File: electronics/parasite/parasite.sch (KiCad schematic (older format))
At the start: 24 parts, among them Q1 MMBT3904, Q2 MMBT3904, Q3 AO3407A, U1 E73-2G4M04S1B

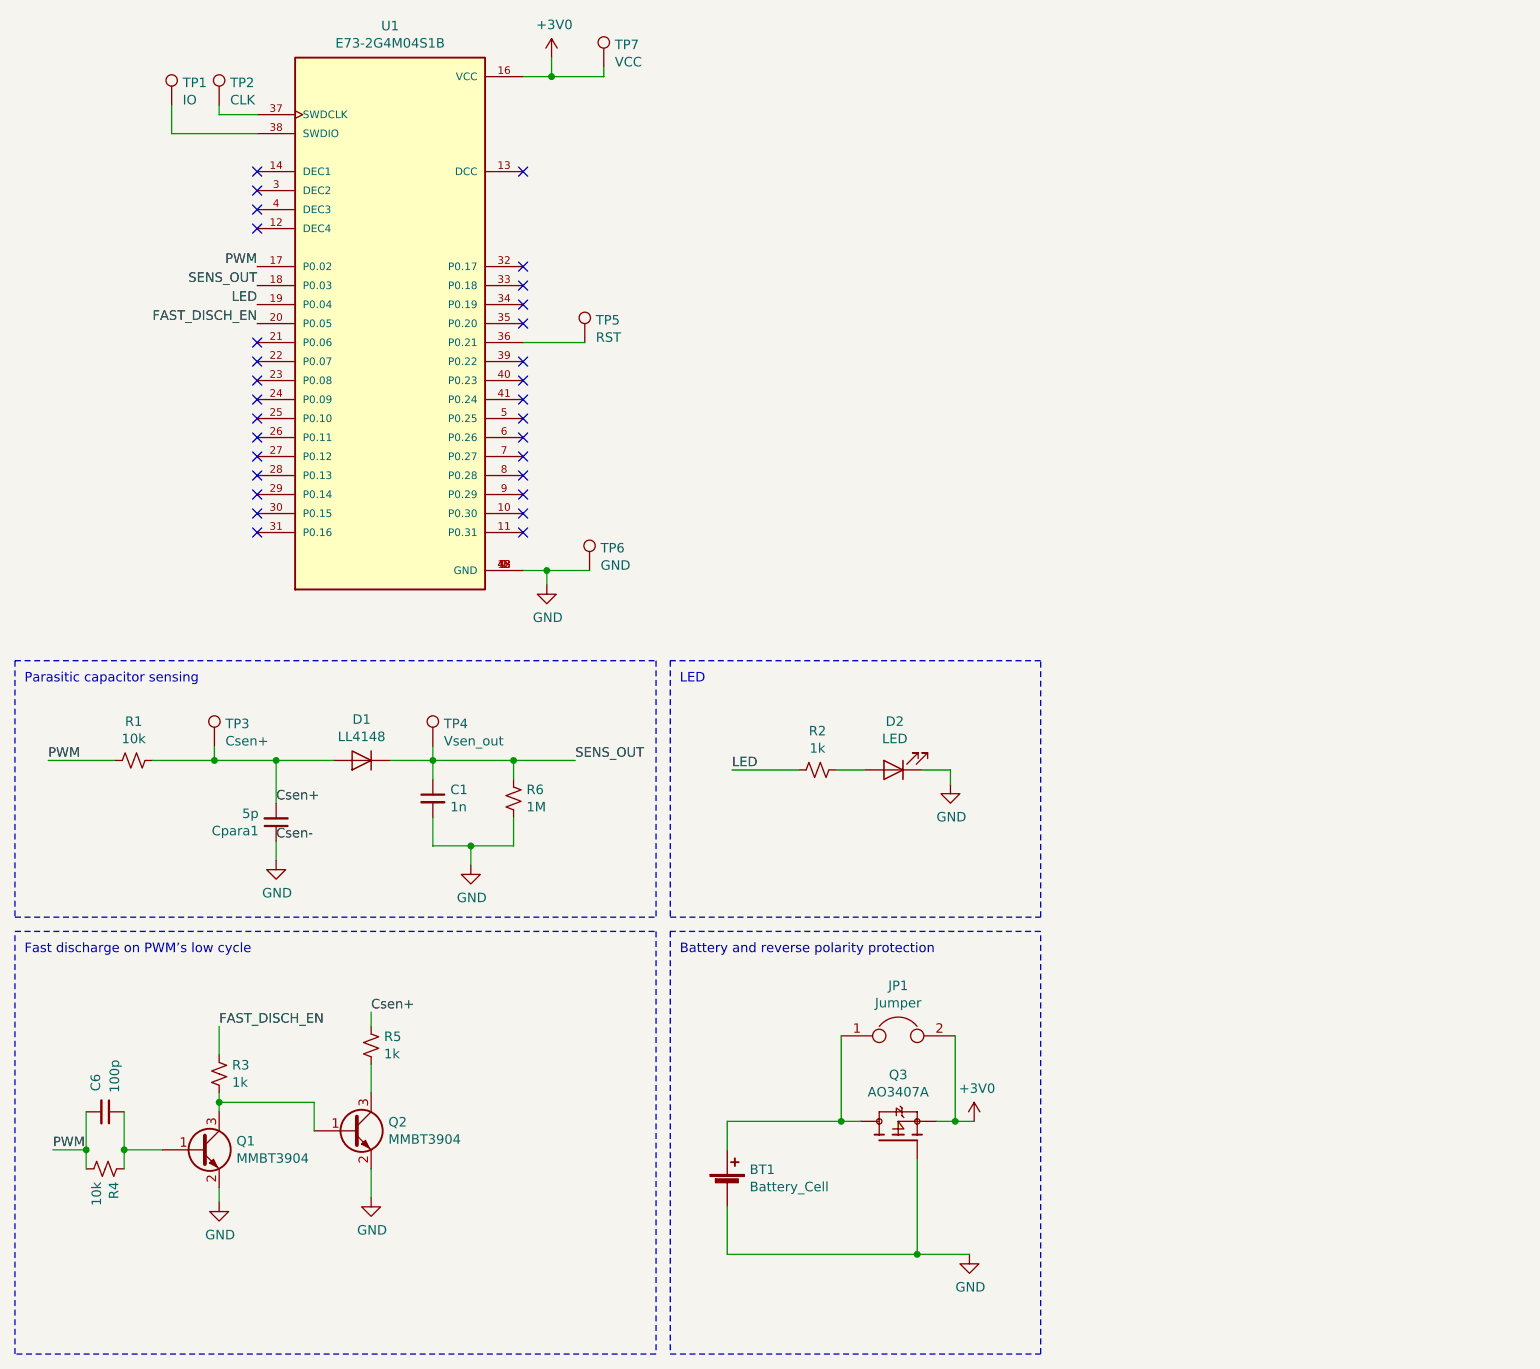
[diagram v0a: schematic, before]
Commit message: Adds sht30 temperature and humidity sensor
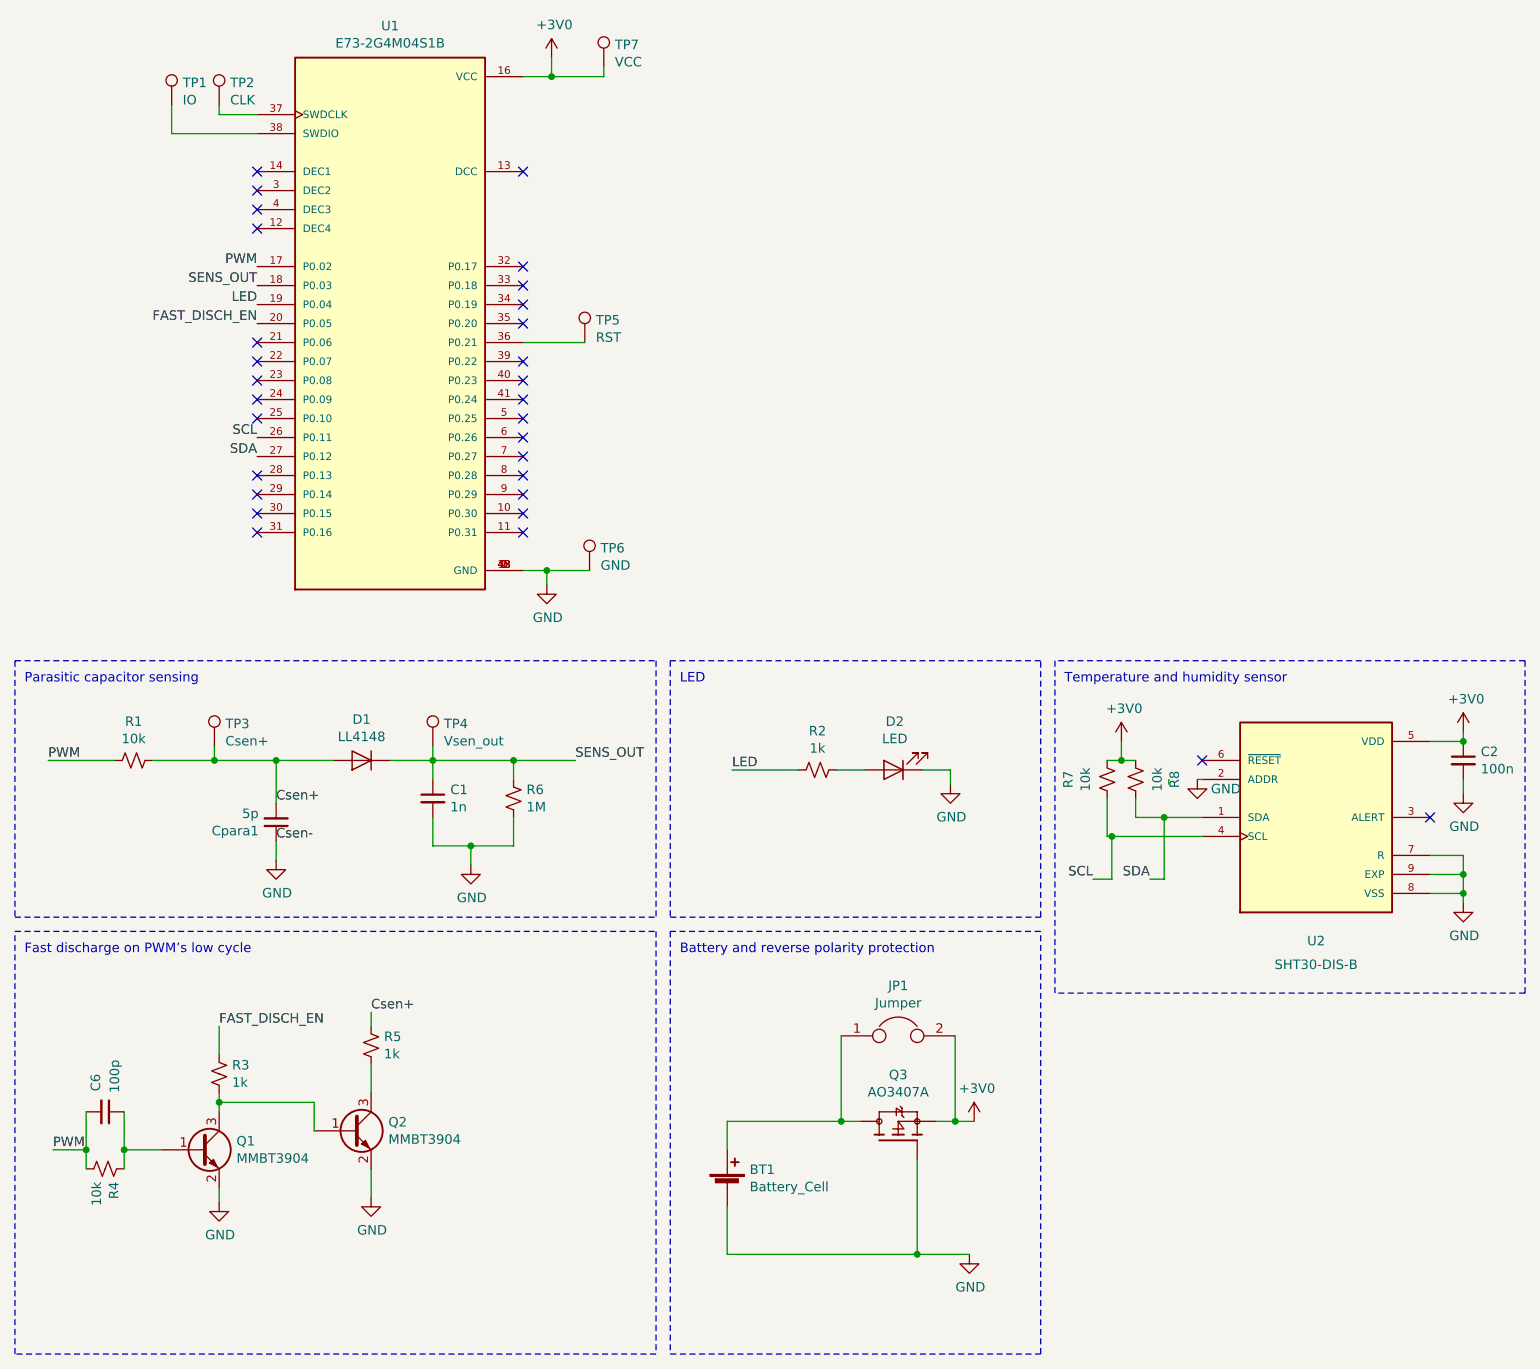
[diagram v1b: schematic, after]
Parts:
- added C2: 100n, Capacitor_SMD:C_0805_2012Metric, symbol Device:C_Small
- added R7, R8: 10k, Resistor_SMD:R_0805_2012Metric, symbol Device:R_Small_US
- added U2: SHT30-DIS-B, DFN250X250X100-9N, symbol SHT30-DIS-B:SHT30-DIS-B
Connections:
- net +3V0: now also C2.1, R7.2, R8.1, U2.5 (VDD)
- net GND: now also C2.2, U2.2 (ADDR), U2.7 (R), U2.8 (VSS), U2.9 (EXP)
- net SCL: now reaches U1.26 (P0.11)
- net SCL: now also R7.1, U2.4 (SCL)
- net SDA: now reaches U1.27 (P0.12)
- net SDA: now also R8.2, U2.1 (SDA)
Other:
- note added: "Temperature and humidity sensor"
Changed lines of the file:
@@
 NoConn ~ 1950 2650
 NoConn ~ 1950 2750
-NoConn ~ 1950 2850
-NoConn ~ 1950 2950
 NoConn ~ 1950 3050
 NoConn ~ 1950 3150
@@
 	1    0    0    -1
 $EndComp
+$Comp
+L SHT30-DIS-B:SHT30-DIS-B U2
+U 1 1 603581DD
+P 7525 4850
+F 0 "U2" H 7525 4200 50  0000 C CNN
+F 1 "SHT30-DIS-B" H 7525 4075 50  0000 C CNN
+F 2 "DFN250X250X100-9N" H 7525 4850 50  0001 L BNN
+F 3 "" H 7525 4850 50  0001 L BNN
+F 4 "Sensirion" H 7525 4850 50  0001 L BNN "MANUFACTURER"
+	1    7525 4850
+	1    0    0    -1
+$EndComp
+$Comp
+L power:+3V0 #PWR0106
+U 1 1 60359DB4
+P 8300 4400
+F 0 "#PWR0106" H 8300 4250 50  0001 C CNN
+F 1 "+3V0" H 8315 4573 50  0000 C CNN
+F 2 "" H 8300 4400 50  0001 C CNN
+F 3 "" H 8300 4400 50  0001 C CNN
+	1    8300 4400
+	1    0    0    -1
+$EndComp
+Wire Wire Line
+	8125 4450 8300 4450
+Wire Wire Line
+	8300 4450 8300 4400
+$Comp
+L power:GND #PWR0107
+U 1 1 6035C6F6
+P 8300 5300
+F 0 "#PWR0107" H 8300 5050 50  0001 C CNN
+F 1 "GND" H 8305 5127 50  0000 C CNN
+F 2 "" H 8300 5300 50  0001 C CNN
+F 3 "" H 8300 5300 50  0001 C CNN
+	1    8300 5300
+	1    0    0    -1
+$EndComp
+Wire Wire Line
+	8125 5250 8300 5250
+Wire Wire Line
+	8300 5250 8300 5300
+Wire Wire Line
+	8125 5050 8300 5050
+Wire Wire Line
+	8300 5050 8300 5150
+Connection ~ 8300 5250
+Wire Wire Line
+	8125 5150 8300 5150
+Connection ~ 8300 5150
+Wire Wire Line
+	8300 5150 8300 5250
+$Comp
+L power:GND #PWR0108
+U 1 1 60360ACA
+P 6900 4650
+F 0 "#PWR0108" H 6900 4400 50  0001 C CNN
+F 1 "GND" H 7050 4600 50  0000 C CNN
+F 2 "" H 6900 4650 50  0001 C CNN
+F 3 "" H 6900 4650 50  0001 C CNN
+	1    6900 4650
+	1    0    0    -1
+$EndComp
+NoConn ~ 6925 4550
+NoConn ~ 8125 4850
+Text Label 1950 2950 2    50   ~ 0
+SDA
+Text Label 1950 2850 2    50   ~ 0
+SCL
+Text Label 6350 5175 2    50   ~ 0
+SCL
+Wire Notes Line
+	8625 4025 6150 4025
+Text Notes 6200 4150 0    50   ~ 0
+Temperature and humidity sensor
+$Comp
+L Device:C_Small C2
+U 1 1 6036F153
+P 8300 4550
+F 0 "C2" H 8392 4596 50  0000 L CNN
+F 1 "100n" H 8392 4505 50  0000 L CNN
+F 2 "Capacitor_SMD:C_0805_2012Metric" H 8300 4550 50  0001 C CNN
+F 3 "~" H 8300 4550 50  0001 C CNN
+	1    8300 4550
+	1    0    0    -1
+$EndComp
+Connection ~ 8300 4450
+$Comp
+L power:GND #PWR0109
+U 1 1 6036FCD2
+P 8300 4725
+F 0 "#PWR0109" H 8300 4475 50  0001 C CNN
+F 1 "GND" H 8305 4552 50  0000 C CNN
+F 2 "" H 8300 4725 50  0001 C CNN
+F 3 "" H 8300 4725 50  0001 C CNN
+	1    8300 4725
+	1    0    0    -1
+$EndComp
+Wire Wire Line
+	8300 4650 8300 4725
+$Comp
+L Device:R_Small_US R8
+U 1 1 60372D0F
+P 6575 4650
+F 0 "R8" V 6780 4650 50  0000 C CNN
+F 1 "10k" V 6689 4650 50  0000 C CNN
+F 2 "Resistor_SMD:R_0805_2012Metric" V 6505 4650 50  0001 C CNN
+F 3 "~" H 6575 4650 50  0001 C CNN
+	1    6575 4650
+	1    0    0    -1
+$EndComp
+$Comp
+L Device:R_Small_US R7
+U 1 1 6037481E
+P 6425 4650
+F 0 "R7" V 6630 4650 50  0000 C CNN
+F 1 "10k" V 6539 4650 50  0000 C CNN
+F 2 "Resistor_SMD:R_0805_2012Metric" V 6355 4650 50  0001 C CNN
+F 3 "~" H 6425 4650 50  0001 C CNN
+	1    6425 4650
+	-1   0    0    1
+$EndComp
+Wire Wire Line
+	6425 4550 6500 4550
+Wire Wire Line
+	6500 4550 6500 4450
+Connection ~ 6500 4550
+Wire Wire Line
+	6500 4550 6575 4550
+$Comp
+L power:+3V0 #PWR0112
+U 1 1 6037C985
+P 6500 4450
+F 0 "#PWR0112" H 6500 4300 50  0001 C CNN
+F 1 "+3V0" H 6515 4623 50  0000 C CNN
+F 2 "" H 6500 4450 50  0001 C CNN
+F 3 "" H 6500 4450 50  0001 C CNN
+	1    6500 4450
+	1    0    0    -1
+$EndComp
+Wire Wire Line
+	6925 4650 6900 4650
+Wire Wire Line
+	6750 4650 6750 4675
+Wire Wire Line
+	6575 4850 6575 4750
+Wire Wire Line
+	6925 4950 6450 4950
+Wire Wire Line
+	6425 4950 6425 4750
+Text Label 6650 5175 2    50   ~ 0
+SDA
+Wire Wire Line
+	6450 5175 6450 4950
+Connection ~ 6450 4950
+Wire Wire Line
+	6450 4950 6425 4950
+Wire Wire Line
+	6725 5175 6725 4850
+Wire Wire Line
+	6575 4850 6725 4850
+Connection ~ 6725 4850
+Wire Wire Line
+	6725 4850 6925 4850
+Wire Wire Line
+	6650 5175 6725 5175
+Wire Wire Line
+	6450 5175 6350 5175
+Wire Notes Line
+	8625 5775 6150 5775
+Wire Notes Line
+	6150 4025 6150 5775
+Wire Notes Line
+	8625 4025 8625 5775
 $EndSCHEMATC
